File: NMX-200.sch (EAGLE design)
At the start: 93 parts, among them IC1 AT90USB1287-AU, IC2 AT90USB1287-MU, J1 PJ-002AH, J2 10118193-0001LF, J3 SJ1-2503A, J4 RJHSE-5385-02, J5 SJ1-2503A, J6 SJ1-2503A, Q1 P-CHANNEL_MOSFET, T1 CMPT2369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

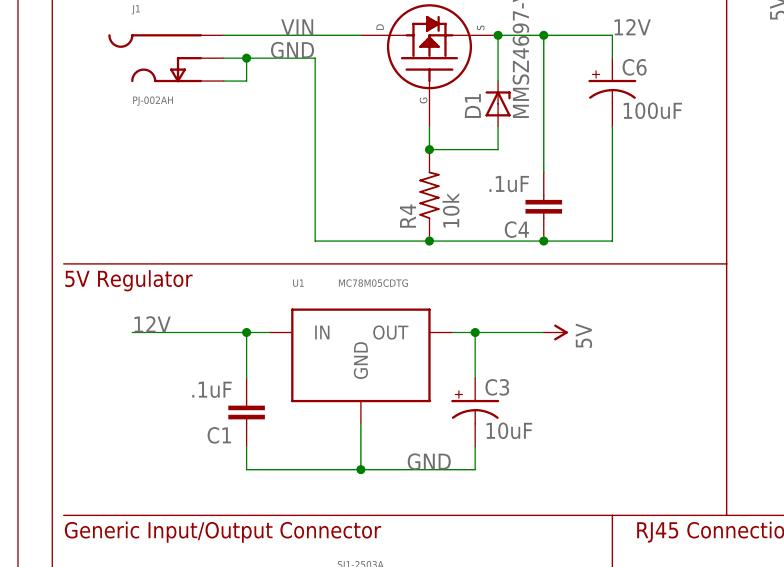
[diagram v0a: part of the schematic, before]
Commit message: Replaced 5V regulator with cold-resistant model
The MC78M05CDTG ON-Semiconductor regulator was replaced with the
MC78M05BDTG. The minimum operating temperature of former is 0°C and the
latter is -45°C. There have been issues connecting to the NMX via
Bluetooth when it is very cold, so this change is being made in an
attempt to address that issue.

The CAM files have not changed at all, but their names have been updated
to Rev 3.
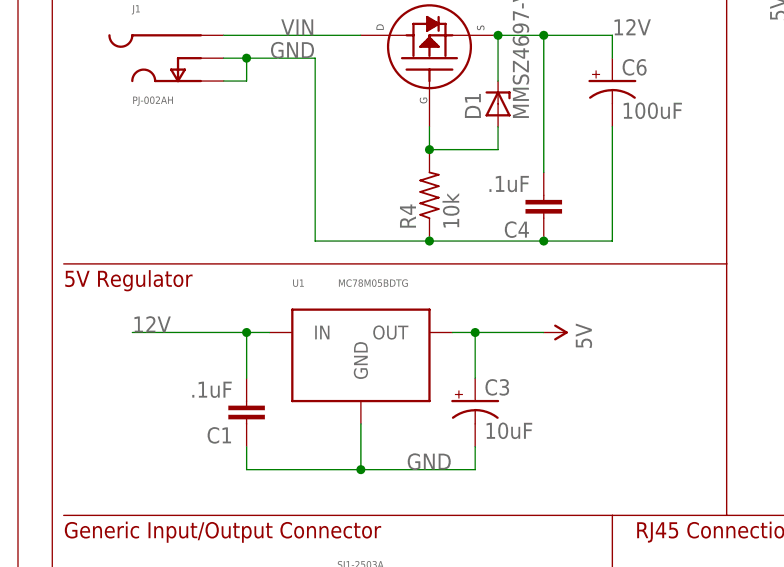
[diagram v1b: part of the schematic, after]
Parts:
- U1: value MC78M05CDTG -> MC78M05BDTG; MPN MC78M05CDTRKG -> MC78M05BDTRKG
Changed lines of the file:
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@@
 <?xml version="1.0" encoding="utf-8"?>
 <!DOCTYPE eagle SYSTEM "eagle.dtd">
-<eagle version="6.6.0">
+<eagle version="6.5.0">
 <drawing>
 <settings>
@@
 <attribute name="MPN" value="RC0402FR-0710KL"/>
 </part>
-<part name="U1" library="QS_Components" deviceset="VOLTAGE_REG" device="" value="MC78M05CDTG">
+<part name="U1" library="QS_Components" deviceset="VOLTAGE_REG" device="" value="MC78M05BDTG">
 <attribute name="MF" value="ON Semiconductor"/>
-<attribute name="MPN" value="MC78M05CDTRKG"/>
+<attribute name="MPN" value="MC78M05BDTRKG"/>
 </part>
 <part name="FB1" library="resistor" deviceset="R-US_" device="R0402" value="HZ0402B102R-10">

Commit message: Changed NMX 200 to 4 layer design
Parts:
- removed IC2: AT90USB1287-MU, at90usb:AT90USB1287-MU
- removed J2: 10118193-0001LF, PP_Connectors:USB10118193-0001LF
- added U$5: USB_CONN, dynamic_perception:USB_CONN
- R19: value 100 -> 14k; MPN RC0402FR-07100RL -> RC0402FR-0714KL
- renumbered U15 to GND
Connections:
- removed net D+: J2.D+, R7.1, U5.IO2
- removed net D-: J2.D-, R6.1, U5.IO1
- removed net USB+: IC1.D+, IC2.D+, R7.2
- removed net USB-: IC1.D-, IC2.D-, R6.2
- new net D_N: R6.1, U$5.D-, U5.IO1
- new net D_P: R7.1, U$5.D+, U5.IO2
- new net USB_N: IC1.D-, R6.2
- new net USB_P: IC1.D+, R7.2
- net 3.3V_EN: no longer IC2.PA0(AD0)
- net 5V: no longer IC2.AVCC, IC2.UVCC, IC2.VCC@1, IC2.VCC@2
- net 5V_USB: now also U$5.+5V; no longer IC2.VBUS, J2.5V
- net AREF: no longer IC2.AREF
- net COM1: no longer IC2.PA2(AD2)
- net COM2: no longer IC2.PE4(INT4/TOSC1)
- net COM3: no longer IC2.PE6(INT6/AIN0)
- net DE: no longer IC2.PD4(ICP1)
- net E-STOP: no longer IC2.PE5(INT5/TOSC2), IC2.PF0(ADC0)
- net FOC: no longer IC2.PB3(PDO/PCINT3/MISO)
- net FOC2: no longer IC2.PB2(PDI/PCINT2/MOSI)
- net GND: now also U$5.GND; no longer IC2.GND@1, IC2.GND@2, IC2.GND@3, IC2.UGND, J2.GND
- net P1_0_5V: no longer IC2.PA1(AD1)
- net PA3: no longer IC2.PA3(AD3)
- net PA4: no longer IC2.PA4(AD4)
- net PA5: no longer IC2.PA5(AD5)
- net PA6: no longer IC2.PA6(AD6)
- net PA7: no longer IC2.PA7(AD7)
- net PB4: no longer IC2.PB4(PCINT4/OC.2A)
- net PB5: no longer IC2.PB5(PCINT5/OC.1A)
- net PB6: no longer IC2.PB6(PCINT6/OC.1B)
- net PB7: no longer IC2.PB7(PCINT7/OC.0A/OC.1C)
- net PC0: no longer IC2.PC0(A8)
- net PC1: no longer IC2.PC1(A9)
- net PC2: no longer IC2.PC2(A10)
- net PC3: no longer IC2.PC3(A11/T.3)
- net PC4: no longer IC2.PC4(A12/OC.3C)
- net PC5: no longer IC2.PC5(A13/OC.3B)
- net PD0: no longer IC2.PD0(OC.0B/SCL/INT0)
- net PD1: no longer IC2.PD1(OC.2B/SDA/INT1)
- net PD5: no longer IC2.PD5(XCK1)
- net PD6: no longer IC2.PD6(T1)
- net PD7: no longer IC2.PD7(T0)
- net PE0: no longer IC2.PE0(/WR)
- net PE1: no longer IC2.PE1(/RD)
- net PE2: no longer IC2.PE2(ALE/HWB)
- net PE3: now also U$5.ID; no longer IC2.PE3(IUID), J2.ID
- net PE7: no longer IC2.PE7(INT7/AIN1/UVCON)
- net PF1: no longer IC2.PF1(ADC1)
- net PF2: no longer IC2.PF2(ADC2)
- net PF3: no longer IC2.PF3(ADC3)
- net PF4: no longer IC2.PF4(ADC4/TCK)
- net PF5: no longer IC2.PF5(ADC5/TMS)
- net PF6: no longer IC2.PF6(ADC6/TDO)
- net PF7: no longer IC2.PF7(ADC7/TDI)
- net RST: no longer IC2.RESET
- net RXA: no longer IC2.PD2(RXD1/INT2)
- net RX_5V: no longer IC2.PC6(A14/OC.3A)
- net SHT: no longer IC2.PB1(PCINT1/SCK)
- net SHT2: no longer IC2.PB0(SS/PCINT0)
- net TXA: no longer IC2.PD3(TXD1/INT3)
- net TX_5V: no longer IC2.PC7(A15/IC.3/CLK0)
- net UCAP: no longer IC2.UCAP
- net XTAL1: no longer IC2.XTAL1
- net XTAL2: no longer IC2.XTAL2
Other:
- note added: "Rev 5"

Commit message: Fixed DRC errors
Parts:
- renumbered GND to U15
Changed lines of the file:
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@@
 <clearance class="0" value="0.1524"/>
 </class>
-<class number="1" name="vcc" width="0.635" drill="0.254">
+<class number="1" name="vcc" width="0.6096" drill="0.254">
 <clearance class="1" value="0.1524"/>
 </class>
-<class number="2" name="gnd" width="0.635" drill="0.254">
+<class number="2" name="gnd" width="0.3048" drill="0.254">
 <clearance class="2" value="0.1524"/>
 </class>
@@
 <attribute name="MPN" value="ACPL-247-500E"/>
 </part>
-<part name="GND" library="QS_Components" deviceset="LMP8640MK" device="">
+<part name="U15" library="QS_Components" deviceset="LMP8640MK" device="">
 <attribute name="MF" value="Texas Instruments"/>
 <attribute name="MPN" value="LMP8640MK-H/NOPB"/>
@@
 <attribute name="MPN" x="68.58" y="48.26" size="1.778" layer="96" rot="R180" display="off"/>
 </instance>
-<instance part="GND" gate="G$1" x="121.92" y="71.12">
+<instance part="U15" gate="G$1" x="121.92" y="71.12">
 <attribute name="MF" x="121.92" y="71.12" size="1.778" layer="96" display="off"/>
 <attribute name="MPN" x="121.92" y="71.12" size="1.778" layer="96" display="off"/>
@@
 </segment>
 <segment>
-<pinref part="GND" gate="G$1" pin="V-"/>
+<pinref part="U15" gate="G$1" pin="V-"/>
 <pinref part="GND34" gate="1" pin="GND"/>
 <wire x1="116.84" y1="58.42" x2="116.84" y2="60.96" width="0.1524" layer="91"/>
@@
 </segment>
 </net>
-<net name="12V" class="1">
+<net name="12V" class="3">
 <segment>
 <wire x1="165.1" y1="142.24" x2="177.8" y2="142.24" width="0.1524" layer="91"/>
@@
 </segment>
 <segment>
-<pinref part="GND" gate="G$1" pin="+IN"/>
+<pinref part="U15" gate="G$1" pin="+IN"/>
 <pinref part="R18" gate="G$1" pin="2"/>
 <wire x1="116.84" y1="78.74" x2="116.84" y2="88.9" width="0.1524" layer="91"/>
@@
 </segment>
 <segment>
-<pinref part="GND" gate="G$1" pin="V+"/>
+<pinref part="U15" gate="G$1" pin="V+"/>
 <pinref part="SUPPLY19" gate="G$1" pin="5V"/>
 <wire x1="134.62" y1="71.12" x2="144.78" y2="71.12" width="0.1524" layer="91"/>
@@
 <net name="N$8" class="0">
 <segment>
-<pinref part="GND" gate="G$1" pin="VOUT"/>
+<pinref part="U15" gate="G$1" pin="VOUT"/>
 <pinref part="R8" gate="G$1" pin="2"/>
 <wire x1="134.62" y1="66.04" x2="137.16" y2="66.04" width="0.1524" layer="91"/>
 </segment>
 </net>
-<net name="12V_MOT" class="1">
+<net name="12V_MOT" class="3">
 <segment>
 <wire x1="144.78" y1="208.28" x2="154.94" y2="208.28" width="0.1524" layer="91"/>
@@
 <segment>
 <pinref part="R18" gate="G$1" pin="1"/>
-<pinref part="GND" gate="G$1" pin="-IN"/>
+<pinref part="U15" gate="G$1" pin="-IN"/>
 <wire x1="127" y1="88.9" x2="127" y2="78.74" width="0.1524" layer="91"/>
 <wire x1="127" y1="78.74" x2="124.46" y2="78.74" width="0.1524" layer="91"/>

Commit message: Added fiducials to bottom of NMX-200
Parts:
- added U$6, U$7: FIDUCIAL, adafruit:FIDUCIAL
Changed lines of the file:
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@@
 </part>
 <part name="U$5" library="dynamic_perception" deviceset="USB_CONN" device=""/>
+<part name="U$6" library="adafruit" deviceset="FIDUCIAL" device=""/>
+<part name="U$7" library="adafruit" deviceset="FIDUCIAL" device=""/>
 </parts>
 <sheets>
@@
 </instance>
 <instance part="U$5" gate="G$1" x="12.7" y="134.62"/>
+<instance part="U$6" gate="G$1" x="200.66" y="175.26"/>
+<instance part="U$7" gate="G$1" x="200.66" y="167.64"/>
 </instances>
 <busses>

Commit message: Fixed some ERC errors, switched to OSHPark DRC
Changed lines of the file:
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@@
 <pinref part="IC1" gate="G$1" pin="XTAL1"/>
 <pinref part="U9" gate="G$1" pin="3"/>
-<wire x1="299.72" y1="220.98" x2="266.7" y2="220.98" width="0.1524" layer="91"/>
+<wire x1="299.72" y1="220.98" x2="276.86" y2="220.98" width="0.1524" layer="91"/>
+<wire x1="276.86" y1="220.98" x2="276.86" y2="226.06" width="0.1524" layer="91"/>
+<wire x1="276.86" y1="226.06" x2="270.002" y2="226.06" width="0.1524" layer="91"/>
+<wire x1="270.002" y1="226.06" x2="270.002" y2="220.98" width="0.1524" layer="91"/>
+<wire x1="270.002" y1="220.98" x2="266.7" y2="220.98" width="0.1524" layer="91"/>
 <pinref part="C9" gate="G$1" pin="1"/>
 <wire x1="261.62" y1="220.98" x2="266.7" y2="220.98" width="0.1524" layer="91"/>
@@
 <pinref part="IC1" gate="G$1" pin="XTAL2"/>
 <wire x1="299.72" y1="223.52" x2="279.4" y2="223.52" width="0.1524" layer="91"/>
-<wire x1="279.4" y1="223.52" x2="279.4" y2="236.22" width="0.1524" layer="91"/>
+<wire x1="279.4" y1="223.52" x2="279.4" y2="228.6" width="0.1524" layer="91"/>
 <pinref part="U9" gate="G$1" pin="1"/>
-<wire x1="266.7" y1="236.22" x2="279.4" y2="236.22" width="0.1524" layer="91"/>
+<wire x1="266.7" y1="236.22" x2="270.002" y2="236.22" width="0.1524" layer="91"/>
+<wire x1="270.002" y1="236.22" x2="270.002" y2="228.6" width="0.1524" layer="91"/>
+<wire x1="270.002" y1="228.6" x2="279.4" y2="228.6" width="0.1524" layer="91"/>
 <pinref part="C8" gate="G$1" pin="1"/>
 <wire x1="266.7" y1="236.22" x2="261.62" y2="236.22" width="0.1524" layer="91"/>
@@
 </sheet>
 </sheets>
+<errors>
+</errors>
 </schematic>
 </drawing>

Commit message: Changed several resistor values to reduce unique part count
See NMX-200 / NMX-201 BOM Google doc change log for 12/15/16 for
details.
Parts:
- R13, R14, R2, R3: value 180 -> 120
- R19: value 14k -> 10k
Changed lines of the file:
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@@
 <attribute name="MPN" value="RC0402JR-075K1L"/>
 </part>
-<part name="R3" library="resistor" deviceset="R-US_" device="R0402" value="180">
-<attribute name="MF" value="Yageo"/>
-<attribute name="MPN" value="RC0402FR-07180RL"/>
-</part>
-<part name="R2" library="resistor" deviceset="R-US_" device="R0402" value="180">
+<part name="R3" library="resistor" deviceset="R-US_" device="R0402" value="120">
+<attribute name="MF" value="Yageo"/>
+<attribute name="MPN" value="RC0402FR-07180RL"/>
+</part>
+<part name="R2" library="resistor" deviceset="R-US_" device="R0402" value="120">
 <attribute name="MF" value="Yageo"/>
 <attribute name="MPN" value="RC0402FR-07180RL"/>
@@
 <attribute name="MPN" value="LTST-S270TBKT"/>
 </part>
-<part name="R19" library="resistor" deviceset="R-US_" device="R0402" value="14k">
+<part name="R19" library="resistor" deviceset="R-US_" device="R0402" value="10k">
 <attribute name="MF" value="Yageo"/>
 <attribute name="MPN" value="RC0402FR-0714KL"/>
@@
 <attribute name="MPN" value="RC0402JR-075K1L"/>
 </part>
-<part name="R13" library="resistor" deviceset="R-US_" device="R0402" value="180">
-<attribute name="MF" value="Yageo"/>
-<attribute name="MPN" value="RC0402FR-07180RL"/>
-</part>
-<part name="R14" library="resistor" deviceset="R-US_" device="R0402" value="180">
-<attribute name="MF" value="Yageo"/>
-<attribute name="MPN" value="RC0402FR-07180RL"/>
+<part name="R13" library="resistor" deviceset="R-US_" device="R0402" value="120">
+<attribute name="MF" value="Yageo"/>
+<attribute name="MPN" value="RC0402FR-07180RL"/>
+</part>
+<part name="R14" library="resistor" deviceset="R-US_" device="R0402" value="120">
+<attribute name="MF" value="Yageo"/>
+<attribute name="MPN" value="RC0402FR-07180RL"/>
